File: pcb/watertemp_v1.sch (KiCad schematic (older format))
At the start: 31 parts, among them J1 RN2483 Ext, J2 SWD, J3 I2C, J4 UART1, J5 UART2, U1 LPC11U24FBD48, U2 RN2483, U3 SHT21, U4 LP5907-Q1, U5 DS18B20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

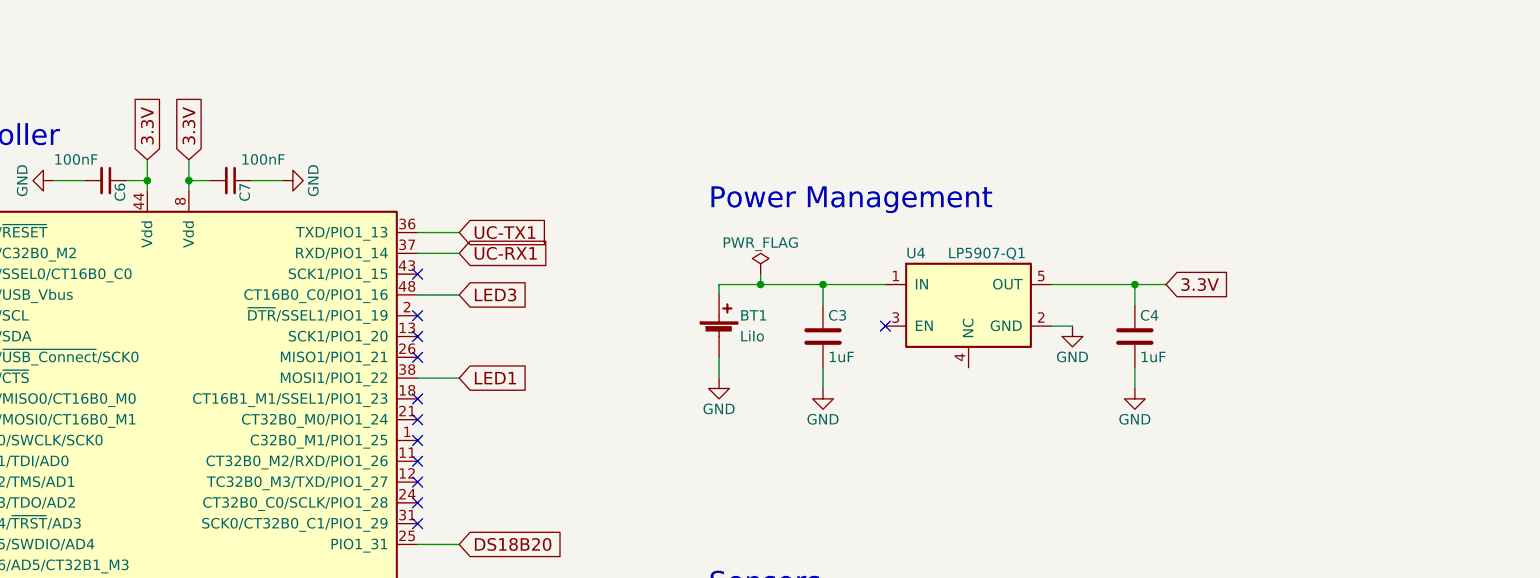
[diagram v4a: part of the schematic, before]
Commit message: Add reverse polarity protection (fixes #11)
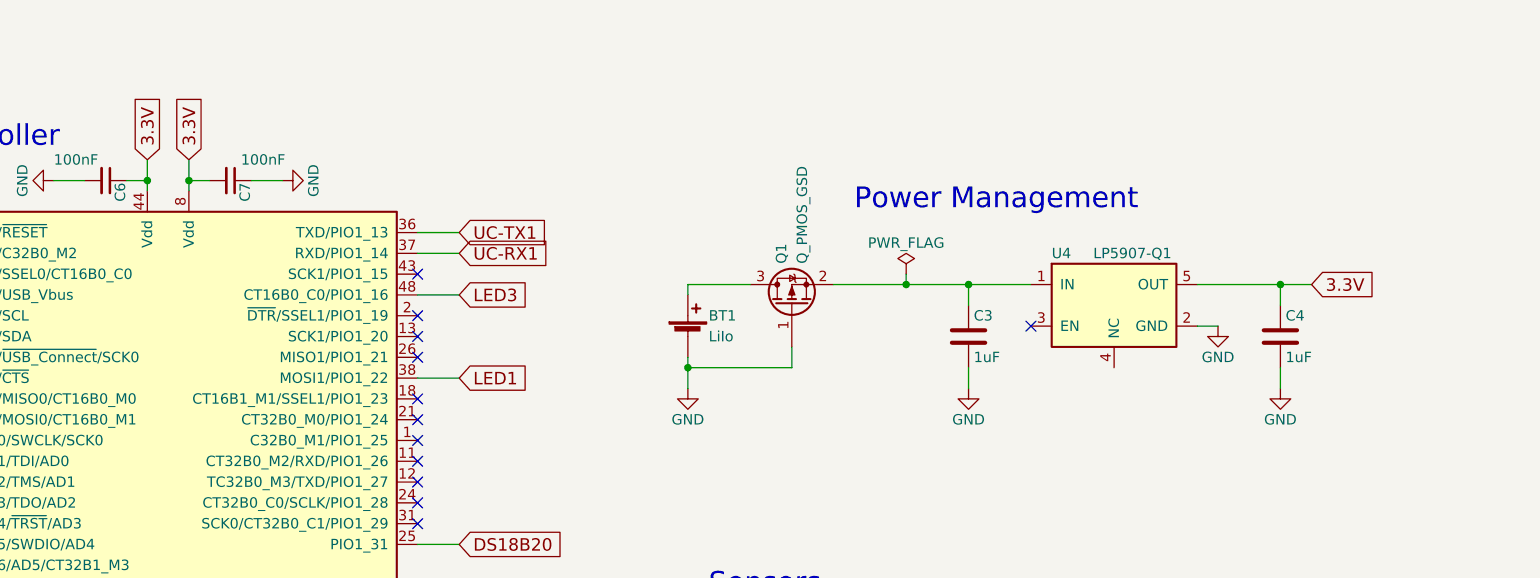
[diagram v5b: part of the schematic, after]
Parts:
- added Q1: Q_PMOS_GSD, TO_SOT_Packages_SMD:SOT-23, symbol Q_PMOS_GSD
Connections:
- net GND: now also Q1.1 (G)
- net at C3.1, U4.1 (IN): now also Q1.2 (S); no longer BT1.1 (+)
- new net: BT1.1 (+), Q1.3 (D)
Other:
- moved on the sheet: BT1, C3, C4, U4
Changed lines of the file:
@@
 L LP5907-Q1 U4
 U 1 1 5935BBE0
-P 6300 1500
-F 0 "U4" H 6000 1750 50  0000 L CNN
-F 1 "LP5907-Q1" H 6200 1750 50  0000 L CNN
-F 2 "TO_SOT_Packages_SMD:SOT-23-6" H 6700 1750 50  0001 L CNN
-F 3 "" H 6300 1500 50  0001 C CNN
-F 4 "296-40365-1-ND" H 6300 1500 60  0001 C CNN "Digikey"
-	1    6300 1500
-	1    0    0    -1
-$EndComp
-Text Notes 5050 1050 0    100  ~ 0
+P 7000 1500
+F 0 "U4" H 6700 1750 50  0000 L CNN
+F 1 "LP5907-Q1" H 6900 1750 50  0000 L CNN
+F 2 "TO_SOT_Packages_SMD:SOT-23-6" H 7400 1750 50  0001 L CNN
+F 3 "" H 7000 1500 50  0001 C CNN
+F 4 "296-40365-1-ND" H 7000 1500 60  0001 C CNN "Digikey"
+	1    7000 1500
+	1    0    0    -1
+$EndComp
+Text Notes 5750 1050 0    100  ~ 0
 Power Management
 $Comp
 L Battery_Cell BT1
 U 1 1 5935BD3B
-P 5100 1650
-F 0 "BT1" H 5200 1750 50  0000 L CNN
-F 1 "LiIo" H 5200 1650 50  0000 L CNN
-F 2 "Battery_Clips:36-54-ND" V 5100 1710 50  0001 C CNN
-F 3 "" V 5100 1710 50  0001 C CNN
-F 4 "36-54-ND" H 5100 1650 60  0001 C CNN "Digikey"
-	1    5100 1650
-	1    0    0    -1
-$EndComp
-NoConn ~ 5900 1600
+P 4950 1650
+F 0 "BT1" H 5050 1750 50  0000 L CNN
+F 1 "LiIo" H 5050 1650 50  0000 L CNN
+F 2 "Battery_Clips:36-54-ND" V 4950 1710 50  0001 C CNN
+F 3 "" V 4950 1710 50  0001 C CNN
+F 4 "36-54-ND" H 4950 1650 60  0001 C CNN "Digikey"
+	1    4950 1650
+	1    0    0    -1
+$EndComp
+NoConn ~ 6600 1600
 $Comp
 L GND #PWR07
 U 1 1 5935BDCA
-P 5100 1850
-F 0 "#PWR07" H 5100 1600 50  0001 C CNN
-F 1 "GND" H 5100 1700 50  0000 C CNN
-F 2 "" H 5100 1850 50  0001 C CNN
-F 3 "" H 5100 1850 50  0001 C CNN
-	1    5100 1850
-	1    0    0    -1
-$EndComp
-Wire Wire Line
-	5100 1850 5100 1750
-Wire Wire Line
-	5100 1450 5100 1400
-Wire Wire Line
-	5100 1400 5900 1400
-Wire Wire Line
-	6700 1400 7250 1400
-Text GLabel 7250 1400 2    60   Input ~ 0
+P 4950 1900
+F 0 "#PWR07" H 4950 1650 50  0001 C CNN
+F 1 "GND" H 4950 1750 50  0000 C CNN
+F 2 "" H 4950 1900 50  0001 C CNN
+F 3 "" H 4950 1900 50  0001 C CNN
+	1    4950 1900
+	1    0    0    -1
+$EndComp
+Wire Wire Line
+	4950 1750 4950 1900
+Wire Wire Line
+	4950 1450 4950 1400
+Wire Wire Line
+	5650 1400 6600 1400
+Wire Wire Line
+	7400 1400 7950 1400
+Text GLabel 7950 1400 2    60   Input ~ 0
 3.3V
 $Comp
 L GND #PWR08
 U 1 1 5935BF9C
-P 6800 1600
-F 0 "#PWR08" H 6800 1350 50  0001 C CNN
-F 1 "GND" H 6800 1450 50  0000 C CNN
-F 2 "" H 6800 1600 50  0001 C CNN
-F 3 "" H 6800 1600 50  0001 C CNN
-	1    6800 1600
-	1    0    0    -1
-$EndComp
-Wire Wire Line
-	6800 1600 6700 1600
+P 7500 1600
+F 0 "#PWR08" H 7500 1350 50  0001 C CNN
+F 1 "GND" H 7500 1450 50  0000 C CNN
+F 2 "" H 7500 1600 50  0001 C CNN
+F 3 "" H 7500 1600 50  0001 C CNN
+	1    7500 1600
+	1    0    0    -1
+$EndComp
+Wire Wire Line
+	7500 1600 7400 1600
 Text Notes 900  750  0    100  ~ 0
 Microcontroller
@@
 L C C3
 U 1 1 5935C5A0
-P 5600 1650
-F 0 "C3" H 5625 1750 50  0000 L CNN
-F 1 "1uF" H 5625 1550 50  0000 L CNN
-F 2 "Capacitors_SMD:C_0805_HandSoldering" H 5638 1500 50  0001 C CNN
-F 3 "" H 5600 1650 50  0001 C CNN
-F 4 "1276-6471-1-ND" H 5600 1650 60  0001 C CNN "Digikey"
-F 5 "Samsung CL21B105KOFNNNG" H 5600 1650 60  0001 C CNN "Part"
-	1    5600 1650
-	1    0    0    -1
-$EndComp
-Wire Wire Line
-	5600 1500 5600 1400
-Connection ~ 5600 1400
-Wire Wire Line
-	5600 1800 5600 1900
+P 6300 1650
+F 0 "C3" H 6325 1750 50  0000 L CNN
+F 1 "1uF" H 6325 1550 50  0000 L CNN
+F 2 "Capacitors_SMD:C_0805_HandSoldering" H 6338 1500 50  0001 C CNN
+F 3 "" H 6300 1650 50  0001 C CNN
+F 4 "1276-6471-1-ND" H 6300 1650 60  0001 C CNN "Digikey"
+F 5 "Samsung CL21B105KOFNNNG" H 6300 1650 60  0001 C CNN "Part"
+	1    6300 1650
+	1    0    0    -1
+$EndComp
+Wire Wire Line
+	6300 1500 6300 1400
+Connection ~ 6300 1400
+Wire Wire Line
+	6300 1800 6300 1900
 $Comp
 L GND #PWR09
 U 1 1 5935C646
-P 5600 1900
-F 0 "#PWR09" H 5600 1650 50  0001 C CNN
-F 1 "GND" H 5600 1750 50  0000 C CNN
-F 2 "" H 5600 1900 50  0001 C CNN
-F 3 "" H 5600 1900 50  0001 C CNN
-	1    5600 1900
+P 6300 1900
+F 0 "#PWR09" H 6300 1650 50  0001 C CNN
+F 1 "GND" H 6300 1750 50  0000 C CNN
+F 2 "" H 6300 1900 50  0001 C CNN
+F 3 "" H 6300 1900 50  0001 C CNN
+	1    6300 1900
 	1    0    0    -1
 $EndComp
@@
 L C C4
 U 1 1 5935C7D2
-P 7100 1650
-F 0 "C4" H 7125 1750 50  0000 L CNN
-F 1 "1uF" H 7125 1550 50  0000 L CNN
-F 2 "Capacitors_SMD:C_0805_HandSoldering" H 7138 1500 50  0001 C CNN
-F 3 "" H 7100 1650 50  0001 C CNN
-F 4 "Samsung Samsung CL21B105KOFNNNG" H 7100 1650 60  0001 C CNN "Part"
-F 5 "1276-6471-1-ND" H 7100 1650 60  0001 C CNN "Digikey"
-	1    7100 1650
-	1    0    0    -1
-$EndComp
-Wire Wire Line
-	7100 1800 7100 1900
+P 7800 1650
+F 0 "C4" H 7825 1750 50  0000 L CNN
+F 1 "1uF" H 7825 1550 50  0000 L CNN
+F 2 "Capacitors_SMD:C_0805_HandSoldering" H 7838 1500 50  0001 C CNN
+F 3 "" H 7800 1650 50  0001 C CNN
+F 4 "Samsung Samsung CL21B105KOFNNNG" H 7800 1650 60  0001 C CNN "Part"
+F 5 "1276-6471-1-ND" H 7800 1650 60  0001 C CNN "Digikey"
+	1    7800 1650
+	1    0    0    -1
+$EndComp
+Wire Wire Line
+	7800 1800 7800 1900
 $Comp
 L GND #PWR010
 U 1 1 5935C857
-P 7100 1900
-F 0 "#PWR010" H 7100 1650 50  0001 C CNN
-F 1 "GND" H 7100 1750 50  0000 C CNN
-F 2 "" H 7100 1900 50  0001 C CNN
-F 3 "" H 7100 1900 50  0001 C CNN
-	1    7100 1900
-	1    0    0    -1
-$EndComp
-Wire Wire Line
-	7100 1500 7100 1400
-Connection ~ 7100 1400
+P 7800 1900
+F 0 "#PWR010" H 7800 1650 50  0001 C CNN
+F 1 "GND" H 7800 1750 50  0000 C CNN
+F 2 "" H 7800 1900 50  0001 C CNN
+F 3 "" H 7800 1900 50  0001 C CNN
+	1    7800 1900
+	1    0    0    -1
+$EndComp
+Wire Wire Line
+	7800 1500 7800 1400
+Connection ~ 7800 1400
 Text GLabel 2350 800  1    60   Input ~ 0
 3.3V
@@
 L PWR_FLAG #FLG013
 U 1 1 5936016C
-P 5300 1350
-F 0 "#FLG013" H 5300 1425 50  0001 C CNN
-F 1 "PWR_FLAG" H 5300 1500 50  0000 C CNN
-F 2 "" H 5300 1350 50  0001 C CNN
-F 3 "" H 5300 1350 50  0001 C CNN
-	1    5300 1350
-	1    0    0    -1
-$EndComp
-Wire Wire Line
-	5300 1350 5300 1400
-Connection ~ 5300 1400
+P 6000 1350
+F 0 "#FLG013" H 6000 1425 50  0001 C CNN
+F 1 "PWR_FLAG" H 6000 1500 50  0000 C CNN
+F 2 "" H 6000 1350 50  0001 C CNN
+F 3 "" H 6000 1350 50  0001 C CNN
+	1    6000 1350
+	1    0    0    -1
+$EndComp
+Wire Wire Line
+	6000 1350 6000 1400
+Connection ~ 6000 1400
 Text Notes 9150 2950 0    100  ~ 0
 JTAG / SWD
@@
 	2550 800  2550 950
 Wire Wire Line
-	2350 950  2350 800
+	2350 800  2350 950
 Wire Wire Line
 	2650 900  2550 900
@@
 	0    1    1    0
 $EndComp
+$Comp
+L Q_PMOS_GSD Q1
+U 1 1 59C0182B
+P 5450 1500
+F 0 "Q1" H 5650 1550 50  0000 L CNN
+F 1 "Q_PMOS_GSD" H 5650 1450 50  0000 L CNN
+F 2 "TO_SOT_Packages_SMD:SOT-23" H 5650 1600 50  0001 C CNN
+F 3 "" H 5450 1500 50  0001 C CNN
+F 4 "SSM3J338RLFCT-ND" H 5450 1500 60  0001 C CNN "Digikey"
+	1    5450 1500
+	0    -1   -1   0
+$EndComp
+Wire Wire Line
+	5450 1800 5450 1700
+Connection ~ 4950 1800
+Wire Wire Line
+	4950 1400 5250 1400
+Wire Wire Line
+	5450 1800 4950 1800
 $EndSCHEMATC

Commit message: Fix oscillator symbol/footprint (fixes #10)
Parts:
- Y1: symbol Crystal -> Crystal_GND24
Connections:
- net GND: now also Y1.2, Y1.4
- net at C1.1, U1.7 (XTALOUT): now also Y1.3; no longer Y1.2
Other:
- moved on the sheet: C1, C2
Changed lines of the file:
@@
 3.3V
 $Comp
-L Crystal Y1
+L Crystal_GND24 Y1
 U 1 1 59359C16
 P 4000 3850
@@
 	1150 3100 1050 3100
 Wire Wire Line
-	3850 3450 3850 4050
-Wire Wire Line
 	3850 3450 3650 3450
 Wire Wire Line
 	3650 3350 4150 3350
 Wire Wire Line
-	4150 3350 4150 4050
+	4150 3350 4150 3850
+Wire Wire Line
+	4150 3850 4350 3850
 Connection ~ 3850 3850
 Connection ~ 4150 3850
@@
 L C C1
 U 1 1 59359F97
-P 3850 4200
-F 0 "C1" H 3875 4300 50  0000 L CNN
-F 1 "18pF" H 3875 4100 50  0000 L CNN
-F 2 "Capacitors_SMD:C_0805" H 3888 4050 50  0001 C CNN
-F 3 "" H 3850 4200 50  0001 C CNN
-F 4 "Samsung CL21C180JBANNNC" H 3850 4200 60  0001 C CNN "Part"
-F 5 "1276-1107-1-ND" H 3850 4200 60  0001 C CNN "Digikey"
-	1    3850 4200
-	1    0    0    -1
-$EndComp
-Wire Wire Line
-	3850 4350 3850 4450
-Wire Wire Line
-	4150 4350 4150 4450
+P 3650 4000
+F 0 "C1" H 3675 4100 50  0000 L CNN
+F 1 "18pF" H 3675 3900 50  0000 L CNN
+F 2 "Capacitors_SMD:C_0805" H 3688 3850 50  0001 C CNN
+F 3 "" H 3650 4000 50  0001 C CNN
+F 4 "Samsung CL21C180JBANNNC" H 3650 4000 60  0001 C CNN "Part"
+F 5 "1276-1107-1-ND" H 3650 4000 60  0001 C CNN "Digikey"
+	1    3650 4000
+	1    0    0    -1
+$EndComp
+Wire Wire Line
+	3650 4150 3650 4250
+Wire Wire Line
+	4350 4150 4350 4250
 $Comp
 L GND #PWR03
 U 1 1 5935A145
-P 4150 4450
-F 0 "#PWR03" H 4150 4200 50  0001 C CNN
-F 1 "GND" H 4150 4300 50  0000 C CNN
-F 2 "" H 4150 4450 50  0001 C CNN
-F 3 "" H 4150 4450 50  0001 C CNN
-	1    4150 4450
+P 4350 4250
+F 0 "#PWR03" H 4350 4000 50  0001 C CNN
+F 1 "GND" H 4350 4100 50  0000 C CNN
+F 2 "" H 4350 4250 50  0001 C CNN
+F 3 "" H 4350 4250 50  0001 C CNN
+	1    4350 4250
 	1    0    0    -1
 $EndComp
@@
 L GND #PWR04
 U 1 1 5935A165
-P 3850 4450
-F 0 "#PWR04" H 3850 4200 50  0001 C CNN
-F 1 "GND" H 3850 4300 50  0000 C CNN
-F 2 "" H 3850 4450 50  0001 C CNN
-F 3 "" H 3850 4450 50  0001 C CNN
-	1    3850 4450
+P 3650 4250
+F 0 "#PWR04" H 3650 4000 50  0001 C CNN
+F 1 "GND" H 3650 4100 50  0000 C CNN
+F 2 "" H 3650 4250 50  0001 C CNN
+F 3 "" H 3650 4250 50  0001 C CNN
+	1    3650 4250
 	1    0    0    -1
 $EndComp
@@
 L C C2
 U 1 1 5975054F
-P 4150 4200
-F 0 "C2" H 4175 4300 50  0000 L CNN
-F 1 "18pF" H 4175 4100 50  0000 L CNN
-F 2 "Capacitors_SMD:C_0805" H 4188 4050 50  0001 C CNN
-F 3 "" H 4150 4200 50  0001 C CNN
-F 4 "Samsung CL21C180JBANNNC" H 4150 4200 60  0001 C CNN "Part"
-F 5 "1276-1107-1-ND" H 4150 4200 60  0001 C CNN "Digikey"
-	1    4150 4200
+P 4350 4000
+F 0 "C2" H 4375 4100 50  0000 L CNN
+F 1 "18pF" H 4375 3900 50  0000 L CNN
+F 2 "Capacitors_SMD:C_0805" H 4388 3850 50  0001 C CNN
+F 3 "" H 4350 4000 50  0001 C CNN
+F 4 "Samsung CL21C180JBANNNC" H 4350 4000 60  0001 C CNN "Part"
+F 5 "1276-1107-1-ND" H 4350 4000 60  0001 C CNN "Digikey"
+	1    4350 4000
 	1    0    0    -1
 $EndComp
@@
 Wire Wire Line
 	5450 1800 4950 1800
+Wire Wire Line
+	3650 3850 3850 3850
+Wire Wire Line
+	3850 3850 3850 3450
+Wire Wire Line
+	4000 4050 4000 4250
+$Comp
+L GND #PWR?
+U 1 1 59C03968
+P 4000 4250
+F 0 "#PWR?" H 4000 4000 50  0001 C CNN
+F 1 "GND" H 4000 4100 50  0000 C CNN
+F 2 "" H 4000 4250 50  0001 C CNN
+F 3 "" H 4000 4250 50  0001 C CNN
+	1    4000 4250
+	1    0    0    -1
+$EndComp
+$Comp
+L GND #PWR?
+U 1 1 59C03B63
+P 4000 3600
+F 0 "#PWR?" H 4000 3350 50  0001 C CNN
+F 1 "GND" H 4000 3450 50  0000 C CNN
+F 2 "" H 4000 3600 50  0001 C CNN
+F 3 "" H 4000 3600 50  0001 C CNN
+	1    4000 3600
+	-1   0    0    1
+$EndComp
+Wire Wire Line
+	4000 3650 4000 3600
 $EndSCHEMATC

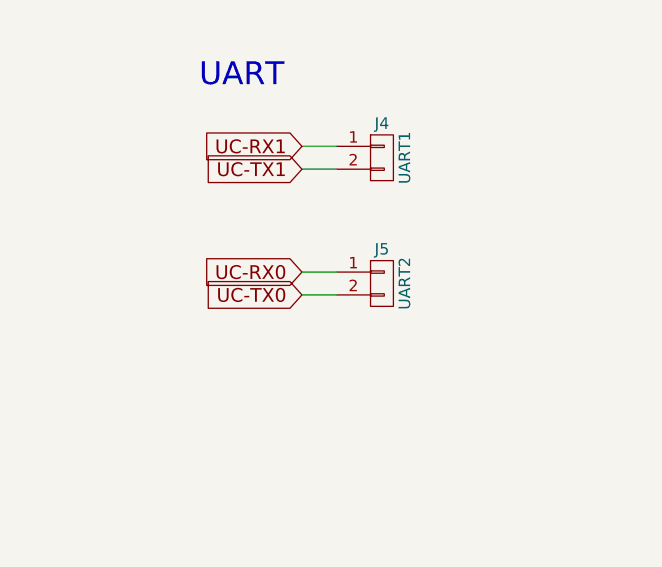
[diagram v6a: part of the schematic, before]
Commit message: Add silkscreen labels to UART headers (fixes #1)
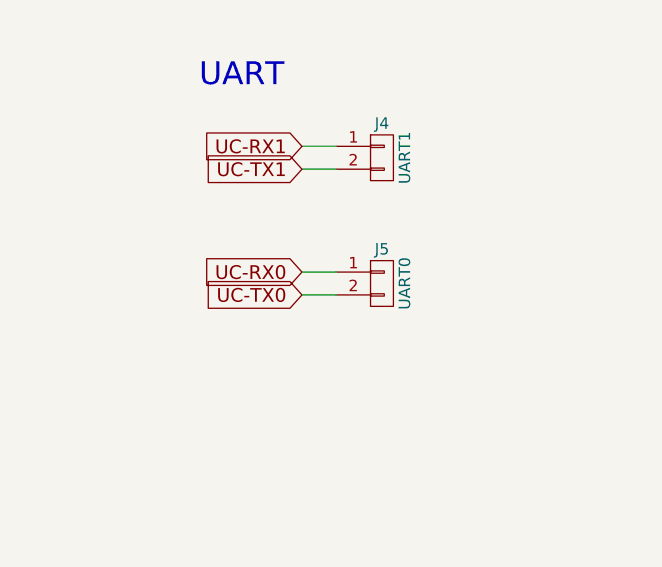
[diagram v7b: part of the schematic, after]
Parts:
- J5: value UART2 -> UART0
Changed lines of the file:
@@
 P 9950 6000
 F 0 "J5" H 9950 6150 50  0000 C CNN
-F 1 "UART2" V 10050 6000 50  0000 C CNN
+F 1 "UART0" V 10050 6000 50  0000 C CNN
 F 2 "Pin_Headers:Pin_Header_Straight_1x02_Pitch2.54mm" H 9950 6000 50  0001 C CNN
 F 3 "" H 9950 6000 50  0001 C CNN

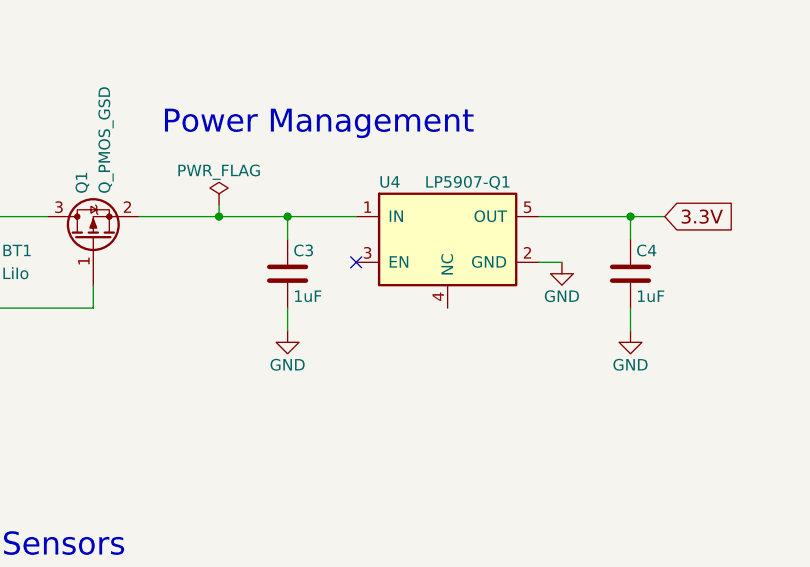
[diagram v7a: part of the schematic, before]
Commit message: Fix problems with LDO
- Use SOT-23-5 footprint (fixes #9)
- Connect EN to IN
- Connect pin 4 (NC) to GND as recommended in the
  datasheet (section 11.2)
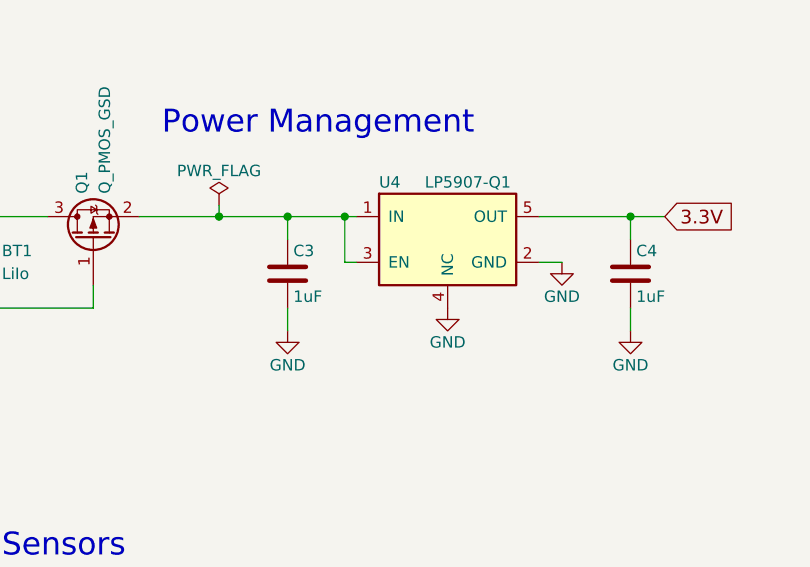
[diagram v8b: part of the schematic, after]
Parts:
- C3, C4: footprint Capacitors_SMD:C_0805_HandSoldering -> Capacitors_SMD:C_0805
- U4: footprint TO_SOT_Packages_SMD:SOT-23-6 -> TO_SOT_Packages_SMD:SOT-23-5
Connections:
- net GND: now also U4.4 (NC)
- net at C3.1, Q1.2 (S), U4.1 (IN): now also U4.3 (EN)
- no-connect marks 50 -> 49
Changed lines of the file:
@@
 F 0 "U4" H 6700 1750 50  0000 L CNN
 F 1 "LP5907-Q1" H 6900 1750 50  0000 L CNN
-F 2 "TO_SOT_Packages_SMD:SOT-23-6" H 7400 1750 50  0001 L CNN
+F 2 "TO_SOT_Packages_SMD:SOT-23-5" H 7400 1750 50  0001 L CNN
 F 3 "" H 7000 1500 50  0001 C CNN
 F 4 "296-40365-1-ND" H 7000 1500 60  0001 C CNN "Digikey"
@@
 	1    0    0    -1
 $EndComp
-NoConn ~ 6600 1600
 $Comp
 L GND #PWR07
@@
 F 0 "C3" H 6325 1750 50  0000 L CNN
 F 1 "1uF" H 6325 1550 50  0000 L CNN
-F 2 "Capacitors_SMD:C_0805_HandSoldering" H 6338 1500 50  0001 C CNN
+F 2 "Capacitors_SMD:C_0805" H 6338 1500 50  0001 C CNN
 F 3 "" H 6300 1650 50  0001 C CNN
 F 4 "1276-6471-1-ND" H 6300 1650 60  0001 C CNN "Digikey"
@@
 F 0 "C4" H 7825 1750 50  0000 L CNN
 F 1 "1uF" H 7825 1550 50  0000 L CNN
-F 2 "Capacitors_SMD:C_0805_HandSoldering" H 7838 1500 50  0001 C CNN
+F 2 "Capacitors_SMD:C_0805" H 7838 1500 50  0001 C CNN
 F 3 "" H 7800 1650 50  0001 C CNN
 F 4 "Samsung Samsung CL21B105KOFNNNG" H 7800 1650 60  0001 C CNN "Part"
@@
 	4000 4050 4000 4250
 $Comp
-L GND #PWR?
+L GND #PWR022
 U 1 1 59C03968
 P 4000 4250
-F 0 "#PWR?" H 4000 4000 50  0001 C CNN
+F 0 "#PWR022" H 4000 4000 50  0001 C CNN
 F 1 "GND" H 4000 4100 50  0000 C CNN
 F 2 "" H 4000 4250 50  0001 C CNN
@@
 $EndComp
 $Comp
-L GND #PWR?
+L GND #PWR023
 U 1 1 59C03B63
 P 4000 3600
-F 0 "#PWR?" H 4000 3350 50  0001 C CNN
+F 0 "#PWR023" H 4000 3350 50  0001 C CNN
 F 1 "GND" H 4000 3450 50  0000 C CNN
 F 2 "" H 4000 3600 50  0001 C CNN
@@
 Wire Wire Line
 	4000 3650 4000 3600
+Wire Wire Line
+	6600 1600 6550 1600
+Wire Wire Line
+	6550 1600 6550 1400
+Connection ~ 6550 1400
+$Comp
+L GND #PWR?
+U 1 1 59D6B3AE
+P 7000 1800
+F 0 "#PWR?" H 7000 1550 50  0001 C CNN
+F 1 "GND" H 7000 1650 50  0000 C CNN
+F 2 "" H 7000 1800 50  0001 C CNN
+F 3 "" H 7000 1800 50  0001 C CNN
+	1    7000 1800
+	1    0    0    -1
+$EndComp
 $EndSCHEMATC
